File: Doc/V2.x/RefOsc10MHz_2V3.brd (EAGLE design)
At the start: 90 x 70 mm, 82 parts, among them CON1 TYCO-AMP_USBUSB-B_SMT, CON2 HEADER-2X5SMD, CON3 SD-73100-0105, CON4 AVR-ISP-6SMD, CON5 AVR-JTAG-10SMD, CON6 HEADER-2X3SMD, CON7 MCX-J-P-X-RA-SM1, U1 ATmega328-P, U2 LC4032V_XXT44, U3 74HCT221D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

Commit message: avr_DF4IAH_Bootloader - Doc - Eagle: 2.1, 2.2, 2.3 - three resistors changed
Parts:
- R311: value 4.7k -> 4.3k
- R611: value 10k -> 15k
- R612: value 45.3k -> 68k
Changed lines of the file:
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@@
 <attribute name="VALUE" x="30.48" y="16.51" size="1.016" layer="27"/>
 </element>
-<element name="R612" library="rcl" package="R0805" value="45.3k" x="46.99" y="40.64" smashed="yes" rot="MR0">
+<element name="R612" library="rcl" package="R0805" value="68k" x="46.99" y="40.64" smashed="yes" rot="MR0">
 <attribute name="NAME" x="45.007865625" y="39.54715625" size="1.016" layer="26" rot="MR180"/>
 <attribute name="VALUE" x="44.79206875" y="42.89283125" size="1.016" layer="28" rot="MR180"/>
 </element>
-<element name="R611" library="rcl" package="R0805" value="10k" x="48.26" y="46.99" smashed="yes" rot="MR90">
+<element name="R611" library="rcl" package="R0805" value="15k" x="48.26" y="46.99" smashed="yes" rot="MR90">
 <attribute name="NAME" x="49.2640875" y="45.7731" size="1.016" layer="26" rot="MR90"/>
 <attribute name="VALUE" x="47.568125" y="48.503196875" size="1.016" layer="28" rot="MR90"/>
@@
 <attribute name="VALUE" x="33.287240625" y="43.547825" size="1.016" layer="27" rot="R90"/>
 </element>
-<element name="R311" library="rcl" package="R0805" value="4.7k" x="20.32" y="11.43" smashed="yes" rot="MR0">
+<element name="R311" library="rcl" package="R0805" value="4.3k" x="20.32" y="11.43" smashed="yes" rot="MR0">
 <attribute name="NAME" x="25.05265625" y="10.7852375" size="1.016" layer="26" rot="MR0"/>
 <attribute name="VALUE" x="18.59439375" y="10.671171875" size="1.016" layer="28" rot="MR0"/>

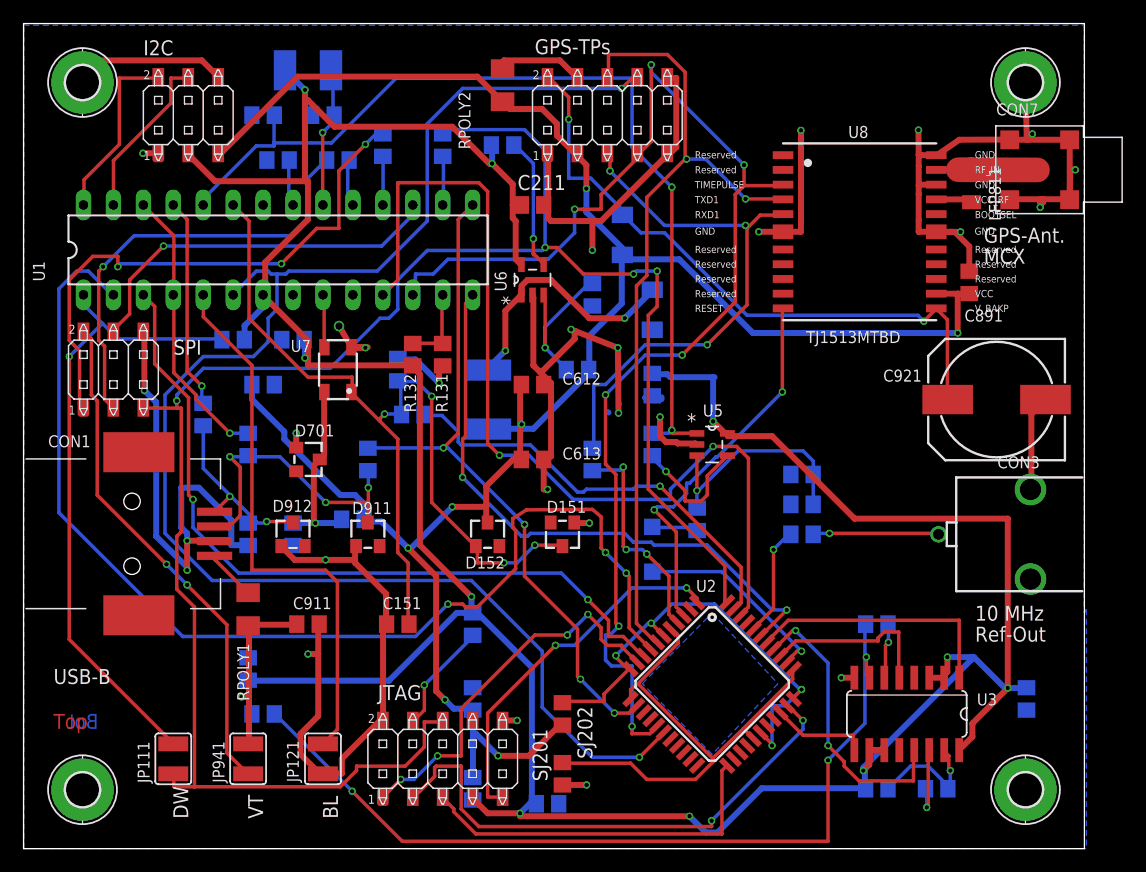
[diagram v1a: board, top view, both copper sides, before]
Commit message: avr_DF4IAH_Bootloader - Doc - Eagle: 2.1, 2.2, 2.3 - misplaced R311 fixed (making short at BL jumper)
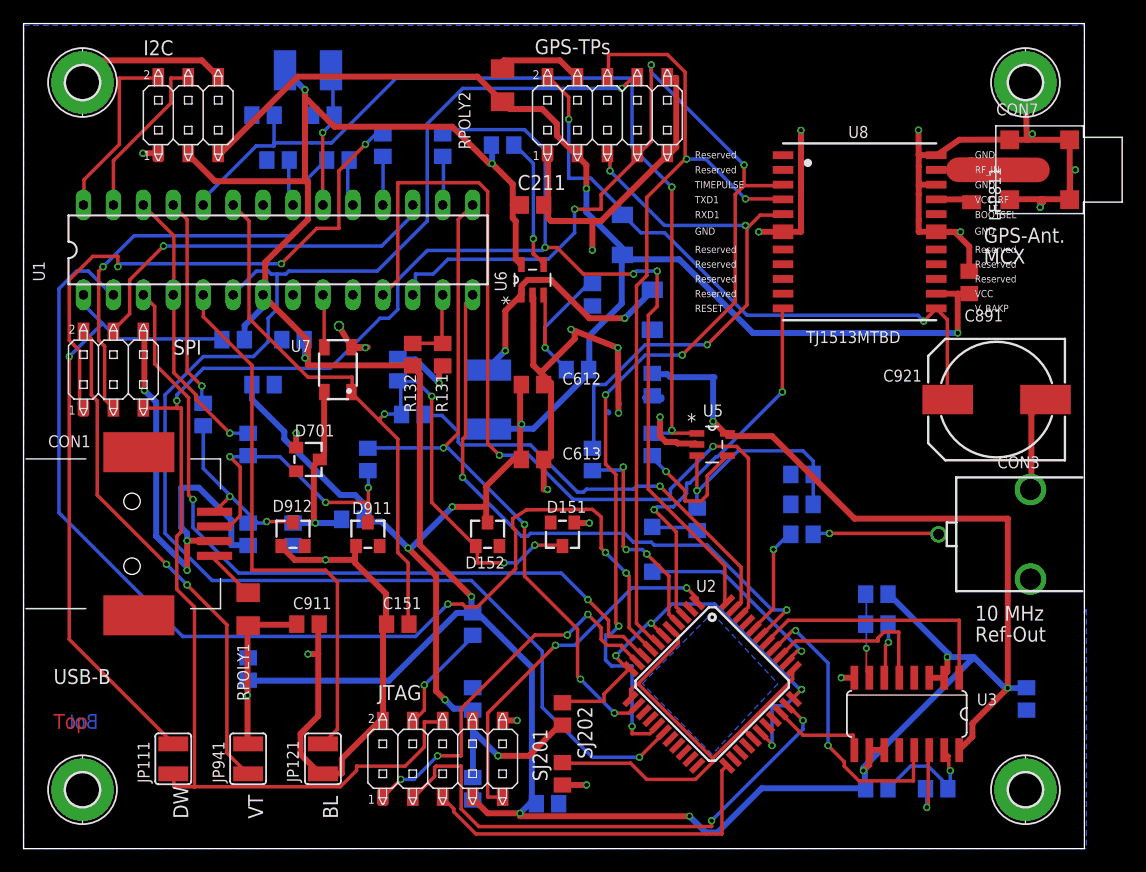
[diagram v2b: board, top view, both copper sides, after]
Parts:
- moved R311 53.1 mm to (72.4, 21.6), turned to 180 degrees
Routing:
- net N$44: track 73.2 -> 7.20 mm, vias 3 -> 1
- net VCC: track 293.9 -> 298.4 mm
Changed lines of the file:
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@@
 </element>
 <element name="C311" library="rcl" package="C0805" value="33p" x="72.39" y="19.05" smashed="yes" rot="MR0">
-<attribute name="NAME" x="77.410903125" y="18.612003125" size="1.016" layer="26" rot="MR0"/>
-<attribute name="VALUE" x="70.3680125" y="18.74570625" size="1.016" layer="28" rot="MR0"/>
+<attribute name="NAME" x="78.350025" y="18.612" size="1.016" layer="26" rot="MR0"/>
+<attribute name="VALUE" x="70.006809375" y="18.5288" size="1.016" layer="28" rot="MR0"/>
 </element>
 <element name="C291" library="rcl" package="C0805" value="100n" x="38.1" y="5.08" smashed="yes" rot="MR270">
@@
 <attribute name="VALUE" x="33.287240625" y="43.547825" size="1.016" layer="27" rot="R90"/>
 </element>
-<element name="R311" library="rcl" package="R0805" value="4.3k" x="20.32" y="11.43" smashed="yes" rot="MR0">
-<attribute name="NAME" x="25.05265625" y="10.7852375" size="1.016" layer="26" rot="MR0"/>
-<attribute name="VALUE" x="18.59439375" y="10.671171875" size="1.016" layer="28" rot="MR0"/>
+<element name="R311" library="rcl" package="R0805" value="4.3k" x="72.39" y="21.59" smashed="yes" rot="MR180">
+<attribute name="NAME" x="78.34014375" y="21.065290625" size="1.016" layer="26" rot="MR0"/>
+<attribute name="VALUE" x="69.931396875" y="21.17753125" size="1.016" layer="28" rot="MR0"/>
 </element>
 <element name="C612" library="rcl" package="C0805" value="22uF" x="43.18" y="39.37" smashed="yes">
@@
 <contactref element="U8" pad="22"/>
 <wire x1="88.75118125" y1="60.143884375" x2="85.111428125" y2="60.143884375" width="0.508" layer="1"/>
-<wire x1="85.111428125" y1="60.143884375" x2="83.46118125" y2="60.143884375" width="0.508" layer="1"/>
+<wire x1="85.111428125" y1="60.143884375" x2="83.700803125" y2="60.143884375" width="0.508" layer="1"/>
 <wire x1="83.46118125" y1="60.143884375" x2="83.700803125" y2="60.143884375" width="0.508" layer="1"/>
 <wire x1="83.700803125" y1="60.143884375" x2="83.664703125" y2="60.13905" width="0.508" layer="1"/>
@@
 <wire x1="83.5" y1="28" x2="70.5" y2="28" width="0.508" layer="1"/>
 <wire x1="83.5" y1="13.625" x2="83.5" y2="28" width="0.508" layer="1"/>
-<wire x1="19.125" y1="11.625" x2="19.125" y2="12.875" width="0.508" layer="16"/>
-<wire x1="19.125" y1="12.875" x2="19.125" y2="14.25" width="0.508" layer="16"/>
-<wire x1="19.25" y1="11.5" x2="19.125" y2="11.625" width="0.508" layer="16"/>
-<wire x1="19.125" y1="14.25" x2="19.05" y2="14.29" width="0.508" layer="16"/>
-<wire x1="19.25" y1="11.5" x2="19.37" y2="11.43" width="0.508" layer="16"/>
 <wire x1="19.125" y1="19" x2="19.05" y2="18.92" width="0.508" layer="1"/>
-<wire x1="19.125" y1="18.75" x2="19.125" y2="12.875" width="0.508" layer="1"/>
-<wire x1="19.125" y1="12.875" x2="19.125" y2="9" width="0.508" layer="1"/>
-<wire x1="19.125" y1="9" x2="19.05" y2="8.89" width="0.508" layer="1"/>
-<wire x1="19.125" y1="18.75" x2="19.05" y2="18.92" width="0.508" layer="1"/>
-<wire x1="18.5" y1="12.875" x2="19.125" y2="12.875" width="0.508" layer="16"/>
-<wire x1="19.125" y1="12.875" x2="18.5" y2="12.875" width="0.508" layer="1"/>
 <wire x1="41.75" y1="50" x2="42.125" y2="49.625" width="0.508" layer="1"/>
 <wire x1="41.75" y1="53.25" x2="41.75" y2="50" width="0.508" layer="1"/>
@@
 <via x="83.5" y="13.625" extent="1-16" drill="0.35"/>
 <via x="78.375" y="16.25" extent="1-16" drill="0.35"/>
-<via x="18.5" y="12.875" extent="1-16" drill="0.35"/>
 <via x="39.75" y="58.125" extent="1-16" drill="0.35"/>
 <via x="42.125" y="3" extent="1-16" drill="0.35"/>
@@
 <wire x1="41.5" y1="54.625" x2="42.125" y2="54.625" width="0.508" layer="1"/>
 <wire x1="42.125" y1="54.625" x2="42.23" y2="54.61" width="0.508" layer="1"/>
+<wire x1="78.5" y1="16.5" x2="73.5" y2="21.5" width="0.508" layer="16"/>
+<wire x1="73.5" y1="21.5" x2="73.34" y2="21.59" width="0.508" layer="16"/>
+<wire x1="78.5" y1="16.5" x2="78.375" y2="16.25" width="0.508" layer="16"/>
+<wire x1="19" y1="18.5" x2="19" y2="13" width="0.508" layer="1"/>
+<wire x1="19" y1="13" x2="19" y2="9" width="0.508" layer="1"/>
+<wire x1="19" y1="9" x2="19.05" y2="8.89" width="0.508" layer="1"/>
+<wire x1="19" y1="18.5" x2="19.05" y2="18.92" width="0.508" layer="1"/>
+<wire x1="19" y1="13" x2="19" y2="14" width="0.508" layer="16"/>
+<wire x1="19" y1="14" x2="19.05" y2="14.29" width="0.508" layer="16"/>
+<via x="19" y="13" extent="1-16" drill="0.3048"/>
 </signal>
 <signal name="N_ADC_PULL">
@@
 <contactref element="C311" pad="2"/>
 <contactref element="R311" pad="1"/>
-<wire x1="27.875" y1="4.875" x2="21.375" y2="11.375" width="0.3" layer="16"/>
-<wire x1="32.125" y1="0.625" x2="27.875" y2="4.875" width="0.3" layer="1"/>
-<wire x1="68.25" y1="0.625" x2="32.125" y2="0.625" width="0.3" layer="1"/>
-<wire x1="68.25" y1="7.5" x2="68.25" y2="0.625" width="0.3" layer="1"/>
-<wire x1="71.375" y1="10.625" x2="68.25" y2="7.5" width="0.3" layer="16"/>
-<wire x1="71.375" y1="19" x2="71.375" y2="16.25" width="0.3" layer="16"/>
-<wire x1="71.375" y1="16.25" x2="71.375" y2="10.625" width="0.3" layer="16"/>
-<wire x1="21.375" y1="11.375" x2="21.27" y2="11.43" width="0.3" layer="16"/>
-<wire x1="71.375" y1="19" x2="71.44" y2="19.05" width="0.3" layer="16"/>
-<wire x1="71.5" y1="14.875" x2="71.75" y2="14.625" width="0.3" layer="1"/>
-<wire x1="71.5" y1="16.25" x2="71.5" y2="14.875" width="0.3" layer="1"/>
-<wire x1="71.75" y1="14.625" x2="71.755" y2="14.5034" width="0.3" layer="1"/>
-<wire x1="71.5" y1="16.25" x2="71.375" y2="16.25" width="0.3" layer="16"/>
-<via x="27.875" y="4.875" extent="1-16" drill="0.35"/>
-<via x="68.25" y="7.5" extent="1-16" drill="0.35"/>
-<via x="71.5" y="16.25" extent="1-16" drill="0.35"/>
+<wire x1="71.5" y1="21.5" x2="71.5" y2="19.5" width="0.1524" layer="16"/>
+<wire x1="71.5" y1="19.5" x2="71.44" y2="19.05" width="0.1524" layer="16"/>
+<wire x1="71.5" y1="21.5" x2="71.44" y2="21.59" width="0.1524" layer="16"/>
+<wire x1="71.5" y1="17" x2="71.5" y2="15" width="0.1524" layer="1"/>
+<wire x1="71.5" y1="19" x2="71.5" y2="17" width="0.1524" layer="16"/>
+<wire x1="71.5" y1="15" x2="71.755" y2="14.5034" width="0.1524" layer="1"/>
+<wire x1="71.5" y1="19" x2="71.44" y2="19.05" width="0.1524" layer="16"/>
+<via x="71.5" y="17" extent="1-16" drill="0.3048"/>
 </signal>
 <signal name="N$45">
